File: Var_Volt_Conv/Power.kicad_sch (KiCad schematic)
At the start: 68 parts, among them J101 Jack-DC, J102 Screw_Terminal_01x02, J103 Screw_Terminal_01x02, Q101 AO3416, Q102 IRFML8244TRPBF, Q103 IRFML8244TRPBF, Q104 AO3407, Q105 AO3407, Q106 AO3407, Q107 AO3407, Q108 AO3416, Q109 AO3416, Q110 AO3416, U101 MCP6541T-I/OT, U102 LM74700, U103 LM74700, U104 TPS62172DSG, U105 TPS552872RYQR, U106 MCP1700T-3002E/TT

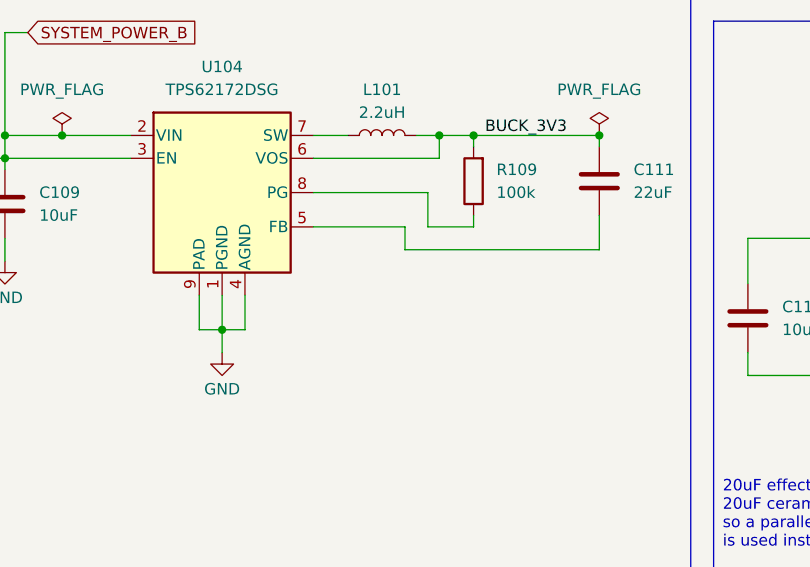
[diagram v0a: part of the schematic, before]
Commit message: Connected FB pin of 3.3V buck converter to ground
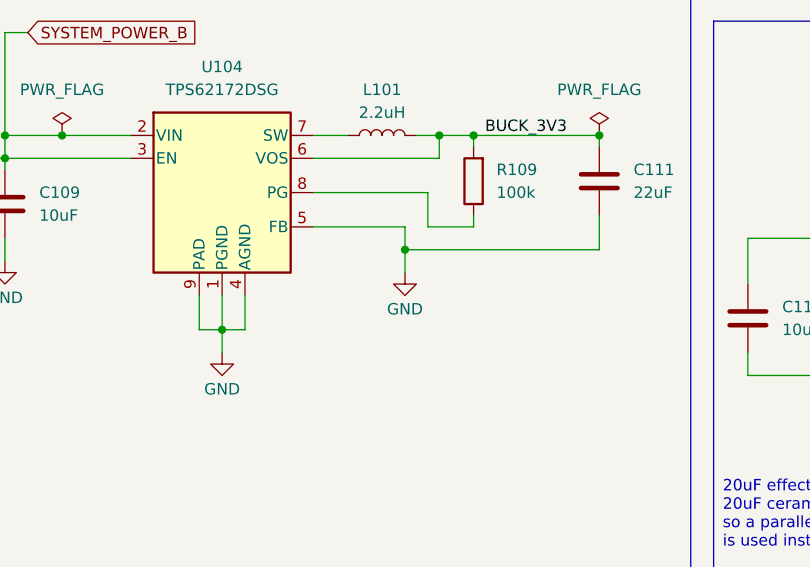
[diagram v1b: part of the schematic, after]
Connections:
- net GND: now also C111.2, U104.5 (FB)
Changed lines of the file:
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@@
 	)
 	(junction
+		(at 196.85 82.55)
+		(diameter 0)
+		(color 0 0 0 0)
+	)
+	(junction
 		(at 271.78 81.28)
 		(diameter 0)
@@
 	(wire
 		(pts
+			(xy 196.85 82.55) (xy 196.85 85.09)
+		)
+		(stroke
+			(width 0)
+			(type default)
+		)
+	)
+	(wire
+		(pts
 			(xy 109.22 57.15) (xy 109.22 45.72)
 		)
@@
 					(unit 1)
 				)
+			)
+		)
+	)
+	(symbol
+		(lib_id "power:GND")
+		(at 196.85 85.09 0)
+		(unit 1)
+		(exclude_from_sim no)
+		(in_bom yes)
+		(on_board yes)
+		(dnp no)
+		(property "Reference" "#PWR0101"
+			(at 196.85 91.44 0)
+			(effects
+				(font
+					(size 1.27 1.27)
+				)
+				(hide yes)
+			)
+		)
+		(property "Value" "GND"
+			(at 196.85 89.154 0)
+			(effects
+				(font
+					(size 1.27 1.27)
+				)
+			)
+		)
+		(property "Footprint" ""
+			(at 196.85 85.09 0)
+			(effects
+				(font
+					(size 1.27 1.27)
+				)
+				(hide yes)
+			)
+		)
+		(property "Datasheet" ""
+			(at 196.85 85.09 0)
+			(effects
+				(font
+					(size 1.27 1.27)
+				)
+				(hide yes)
+			)
+		)
+		(property "Description" "Power symbol creates a global label with name \"GND\" , ground"
+			(at 196.85 85.09 0)
+			(effects
+				(font
+					(size 1.27 1.27)
+				)
+				(hide yes)
+			)
+		)
+		(pin "1"
+		)
+		(instances
+			(project "Var_Volt_Conv"
+				(path "/7c9580d6-c22f-4506-b9c3-9272e882c9fb/18589d04-92b7-4bb3-b941-112d31f9b6cf"
+					(reference "#PWR0101")
+					(unit 1)
+				)

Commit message: Completed rough layout
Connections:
- net ST_PPM_GATE: now reaches C110.1, Q106.1 (G), Q107.1 (G), R107.1, R108.1
- net ST_PPM_SOURCE: now reaches C110.2, Q106.2 (S), Q107.2 (S), R107.2
- net VCAP_J: now reaches C104.2, U102.1 (VCAP)
- net BUCK_PPM_GATE: now reaches C108.1, Q104.1 (G), Q105.1 (G), R104.1, R105.1
- net BUCK_PPM_SOURCE: now reaches C108.2, Q104.2 (S), Q105.2 (S), R105.2
- net BB_FEEDBACK: now reaches R115.2, RV101.2, U105.14 (FB)
- net BB_POT_R: now reaches R117.1, RV101.3
- net POW_IND_LED_R: now reaches D106.1 (K), R113.1
- net POW_IND_R_NMOS: now reaches Q110.3 (D), R113.2
- net COMP_POWER: now reaches C103.1, D103.1 (K), D105.1 (K), U101.5 (V+)
- net ST_3V3_Diode: now reaches D104.1 (K), D105.2 (A)
- net ST_PPM_INV2: now reaches Q108.3 (D), R108.2
- net ST_PPM_IN: now reaches R102.2, R103.1, U101.4 (-)
- net ST_PPM_INV1: now reaches Q108.1 (G), Q109.3 (D), R110.2
- net BB_COMP2: now reaches C121.1, R114.2
- net BB_FSW2: now reaches R111.2, R112.1
- net PG: now reaches R109.1, U104.8 (PG)
- net BB_SW2: now reaches C117.1, L102.2, U105.10 (SW2)
- net BB_COMP1: now reaches C119.1, R114.1, U105.15 (COMP)
- net BB_BOOT2: now reaches C117.2, U105.19 (BOOT2)
- net BB_BOOT1: now reaches C116.2, U105.20 (BOOT1)
- net BB_FSW1: now reaches R111.1, U105.6 (FSW)
- net BB_SW1: now reaches C116.1, L102.1, U105.8 (SW1)
- net VCAP_T: now reaches C105.2, U103.1 (VCAP)
- net BUCK_SW: now reaches L101.1, U104.7 (SW)
- net BUCK_PPM_INV: now reaches Q101.3 (D), R104.2
- net BUCK_3V3 renamed BUCK_VOS
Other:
- moved on the sheet: C116, C117, D103, D104, D106, L101, R109, R111, R112

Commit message: Routed signal traces and made power pours for microcontroller and display, also changed 4.7, 1uF and 2.2uF caps to 0402
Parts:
- C122, C123: footprint Capacitor_SMD:C_0603_1608Metric -> Capacitor_SMD:C_0402_1005Metric
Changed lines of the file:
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@@
 			)
 		)
-		(property "Footprint" "Capacitor_SMD:C_0603_1608Metric"
+		(property "Footprint" "Capacitor_SMD:C_0402_1005Metric"
 			(at 355.2952 182.88 0)
 			(effects
@@
 			)
 		)
-		(property "Footprint" "Capacitor_SMD:C_0603_1608Metric"
+		(property "Footprint" "Capacitor_SMD:C_0402_1005Metric"
 			(at 389.5852 182.88 0)
 			(effects

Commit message: Routed Input system power circuitry, and named the LM74700 gate connection nets
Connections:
- net GATE_J: now reaches Q102.1 (G), U102.5 (GATE)
- net GATE_T: now reaches Q103.1 (G), U103.5 (GATE)
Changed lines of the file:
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@@
+		)
+	)
+	(label "GATE_T"
+		(at 101.6 110.49 0)
+		(fields_autoplaced yes)
+		(effects
+			(font
+				(size 1.27 1.27)
+			)
+			(justify left bottom)
 		)
 	)
@@
 		(fields_autoplaced yes)
 		(effects
+			(font
+				(size 1.27 1.27)
+			)
+			(justify left bottom)
+		)
+	)
+	(label "GATE_J"
+		(at 101.6 55.88 0)
+		(fields_autoplaced yes)
+		(effects

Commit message: Finished tracing priority 3.3V power multiplexer, changed terminal block footprints to 5.00mm pitch
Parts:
- J102, J103: footprint TerminalBlock_4Ucon:TerminalBlock_4Ucon_1x02_P3.50mm_Vertical -> TerminalBlock_Phoenix:TerminalBlock_Phoenix_MKDS-1,5-2_1x02_P5.00mm_Horizontal
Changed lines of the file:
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@@
 			)
 		)
-		(property "Footprint" "TerminalBlock_4Ucon:TerminalBlock_4Ucon_1x02_P3.50mm_Vertical"
+		(property "Footprint" "TerminalBlock_Phoenix:TerminalBlock_Phoenix_MKDS-1,5-2_1x02_P5.00mm_Horizontal"
 			(at 34.29 109.22 0)
 			(effects
@@
 			)
 		)
-		(property "Footprint" "TerminalBlock_4Ucon:TerminalBlock_4Ucon_1x02_P3.50mm_Vertical"
+		(property "Footprint" "TerminalBlock_Phoenix:TerminalBlock_Phoenix_MKDS-1,5-2_1x02_P5.00mm_Horizontal"
 			(at 377.19 81.28 0)
 			(effects

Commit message: Add Power, digital and analog grounds
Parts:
- added NT101: NetTie_3, NetTie:NetTie-3_THT_Pad1.0mm, symbol Device:NetTie_3
- added NT102: NetTie_2, NetTie:NetTie-2_SMD_Pad0.5mm, symbol Device:NetTie_2
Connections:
- net GND: no longer C101.2, C102.2, C103.2, C106.2, C107.2, C109.2, C111.2, C112.2, C113.2, C114.2, C115.2, C118.2, C119.2, C120.2, C121.2, C122.2, C123.2, D101.1 (A1), D102.1 (A1), J101.2, J102.2 (Pin_2), J103.2 (Pin_2), Q101.2 (S), Q108.2 (S), Q109.2 (S), Q110.2 (S), R103.2, R112.2, R117.2, U101.2 (V-), U102.2 (GND), U103.2 (GND), U104.1 (PGND), U104.4 (AGND), U104.5 (FB), U104.9 (PAD), U105.17 (AGND), U105.5 (DITH/SYNC), U105.9 (PGND), U106.1 (GND)
- new net GNDA: C119.2, C121.2, NT101.2, NT102.2, R112.2, R117.2, U105.17 (AGND), U105.5 (DITH/SYNC)
- new net GNDD: NT101.3
- new net GNDPWR: C101.2, C102.2, C103.2, C106.2, C107.2, C109.2, C111.2, C112.2, C113.2, C114.2, C115.2, C118.2, C120.2, C122.2, C123.2, D101.1 (A1), D102.1 (A1), J101.2, J102.2 (Pin_2), J103.2 (Pin_2), NT101.1, NT102.1, Q101.2 (S), Q108.2 (S), Q109.2 (S), Q110.2 (S), R103.2, U101.2 (V-), U102.2 (GND), U103.2 (GND), U104.1 (PGND), U104.4 (AGND), U104.5 (FB), U104.9 (PAD), U105.9 (PGND), U106.1 (GND)

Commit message: Updated power and analog ground connections of the buck converter
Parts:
- added NT103: NetTie_2, NetTie:NetTie-2_SMD_Pad0.5mm, symbol Device:NetTie_2
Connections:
- net GNDA: now also U104.4 (AGND), NT103.2
- net GNDPWR: now also NT103.1; no longer U104.4 (AGND)

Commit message: Labeled subcircuits in PCB
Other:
- title: (none) -> Variable Voltage Controller
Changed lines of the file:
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@@
 	(generator_version "8.0")
 	(paper "A3")
+	(title_block
+		(title "Variable Voltage Controller")
+		(date "2025-02-02")
+		(rev "1.0")
+	)
 	(junction
 		(at 345.44 132.08)
